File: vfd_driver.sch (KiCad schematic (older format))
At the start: 23 parts, among them J1 INPUT, J2 FIL, J3 HV, U1 LM4871, U2 LT1073CS

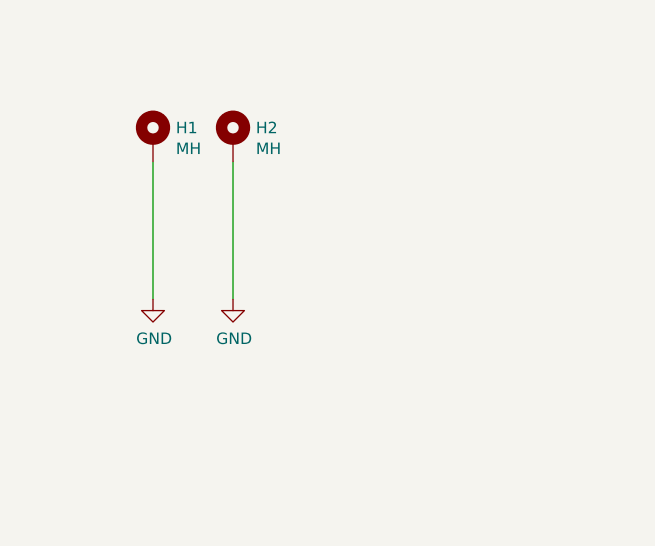
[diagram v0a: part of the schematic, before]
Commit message: add marks that helps, when the board is drilled.
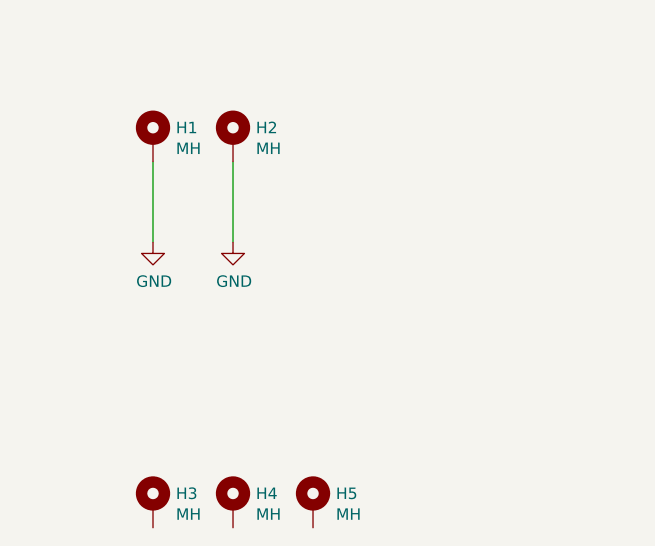
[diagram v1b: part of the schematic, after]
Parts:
- added H3, H4, H5: MH, custom_footprint:markierung, symbol Mechanical:MountingHole_Pad
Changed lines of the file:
@@
 L power:GND #PWR0101
 U 1 1 5C15D6F6
-P 950 5350
-F 0 "#PWR0101" H 950 5100 50  0001 C CNN
-F 1 "GND" H 955 5177 50  0000 C CNN
-F 2 "" H 950 5350 50  0001 C CNN
-F 3 "" H 950 5350 50  0001 C CNN
-	1    950  5350
+P 950 5100
+F 0 "#PWR0101" H 950 4850 50  0001 C CNN
+F 1 "GND" H 955 4927 50  0000 C CNN
+F 2 "" H 950 5100 50  0001 C CNN
+F 3 "" H 950 5100 50  0001 C CNN
+	1    950  5100
 	1    0    0    -1
 $EndComp
@@
 L power:GND #PWR0102
 U 1 1 5C15DD1A
-P 1300 5350
-F 0 "#PWR0102" H 1300 5100 50  0001 C CNN
-F 1 "GND" H 1305 5177 50  0000 C CNN
-F 2 "" H 1300 5350 50  0001 C CNN
-F 3 "" H 1300 5350 50  0001 C CNN
-	1    1300 5350
+P 1300 5100
+F 0 "#PWR0102" H 1300 4850 50  0001 C CNN
+F 1 "GND" H 1305 4927 50  0000 C CNN
+F 2 "" H 1300 5100 50  0001 C CNN
+F 3 "" H 1300 5100 50  0001 C CNN
+	1    1300 5100
 	1    0    0    -1
 $EndComp
@@
 	1    0    0    -1
 $EndComp
-Wire Wire Line
-	950  4750 950  5350
-Wire Wire Line
-	1300 4750 1300 5350
 $Comp
 L Regulator_Switching:LT1073CS U2
@@
 	1500 1450 1500 1750
 $Comp
-L power:+12V #PWR?
+L power:+12V #PWR0104
 U 1 1 5CB2E3D1
 P 2100 1900
-F 0 "#PWR?" H 2100 1750 50  0001 C CNN
+F 0 "#PWR0104" H 2100 1750 50  0001 C CNN
 F 1 "+12V" H 2115 2073 50  0000 C CNN
 F 2 "" H 2100 1900 50  0001 C CNN
@@
 	1    0    0    -1
 $EndComp
+$Comp
+L Mechanical:MountingHole_Pad H3
+U 1 1 5CB28A83
+P 950 6250
+F 0 "H3" H 1050 6299 50  0000 L CNN
+F 1 "MH" H 1050 6208 50  0000 L CNN
+F 2 "custom_footprint:markierung" H 950 6250 50  0001 C CNN
+F 3 "~" H 950 6250 50  0001 C CNN
+	1    950  6250
+	1    0    0    -1
+$EndComp
+Wire Wire Line
+	950  4750 950  5100
+Wire Wire Line
+	1300 4750 1300 5100
+$Comp
+L Mechanical:MountingHole_Pad H4
+U 1 1 5CB2E9A0
+P 1300 6250
+F 0 "H4" H 1400 6299 50  0000 L CNN
+F 1 "MH" H 1400 6208 50  0000 L CNN
+F 2 "custom_footprint:markierung" H 1300 6250 50  0001 C CNN
+F 3 "~" H 1300 6250 50  0001 C CNN
+	1    1300 6250
+	1    0    0    -1
+$EndComp
+$Comp
+L Mechanical:MountingHole_Pad H5
+U 1 1 5CB2E9E6
+P 1650 6250
+F 0 "H5" H 1750 6299 50  0000 L CNN
+F 1 "MH" H 1750 6208 50  0000 L CNN
+F 2 "custom_footprint:markierung" H 1650 6250 50  0001 C CNN
+F 3 "~" H 1650 6250 50  0001 C CNN
+	1    1650 6250
+	1    0    0    -1
+$EndComp
